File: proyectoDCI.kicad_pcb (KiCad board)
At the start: 2 copper layers, 27 parts, among them IC1 AG849, IC2 AD5933, IC3 ASFLMB-16.000MHZ-LY-T, IC4 ADP150, P1 GSG-RF-CONN, P2 GSG-RF-CONN, P3 CONN_02X04, P4 CONN_01X01, U1 AD8606

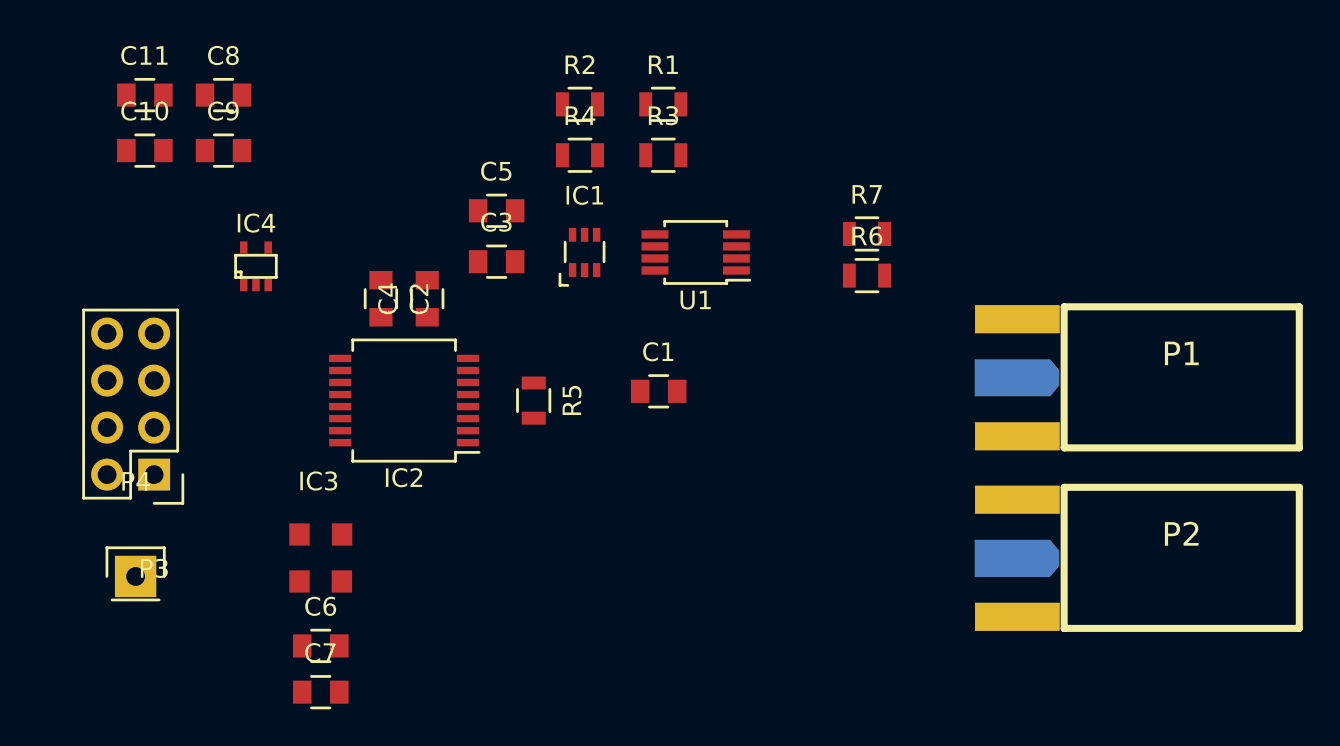
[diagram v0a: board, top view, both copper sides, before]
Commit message: Reformulado el esquematico para contener el diseño en dos hojas
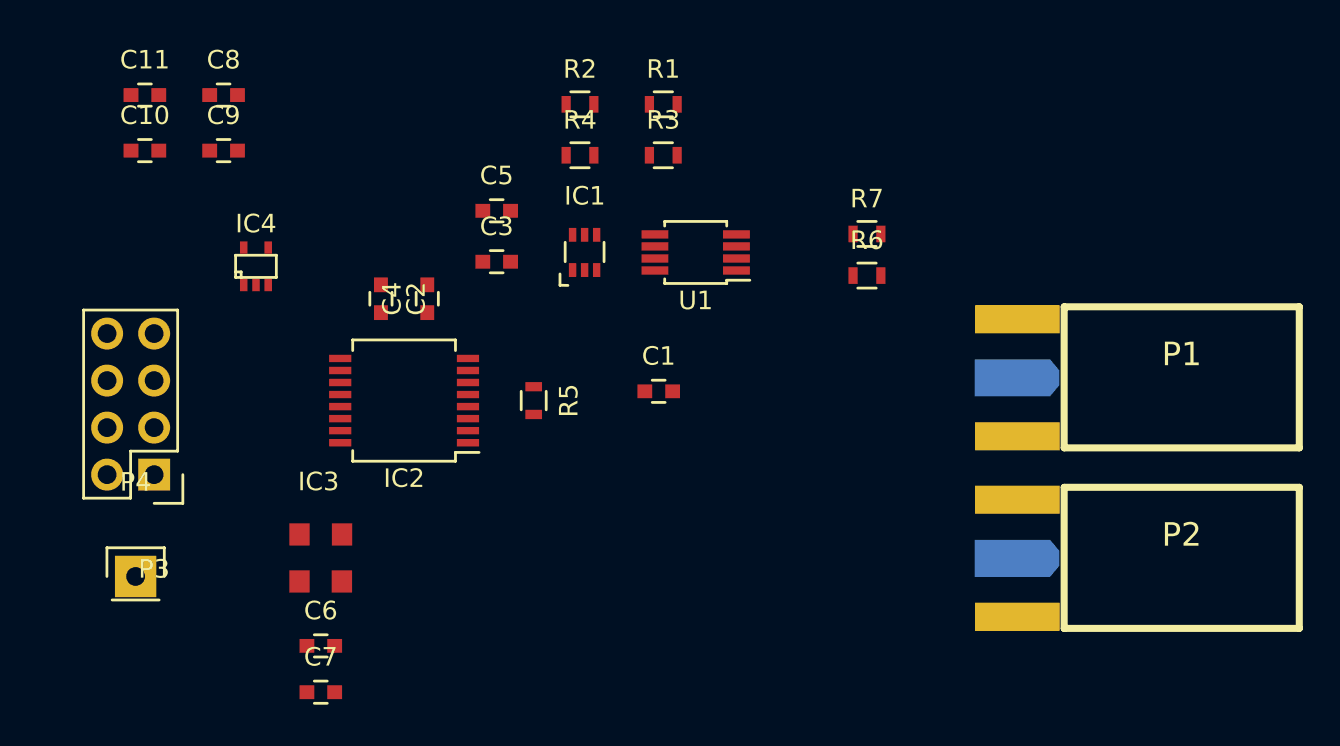
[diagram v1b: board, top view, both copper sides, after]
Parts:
- C1, C10, C11, C2, C3, C4, C5, C6, C7, C8, C9: footprint Capacitors_SMD:C_0805 -> Capacitors_SMD:C_0603
- R1, R2, R3, R4, R5, R6, R7: footprint Resistors_SMD:R_0805 -> Resistors_SMD:R_0603

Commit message: Problema de footprints solucionado
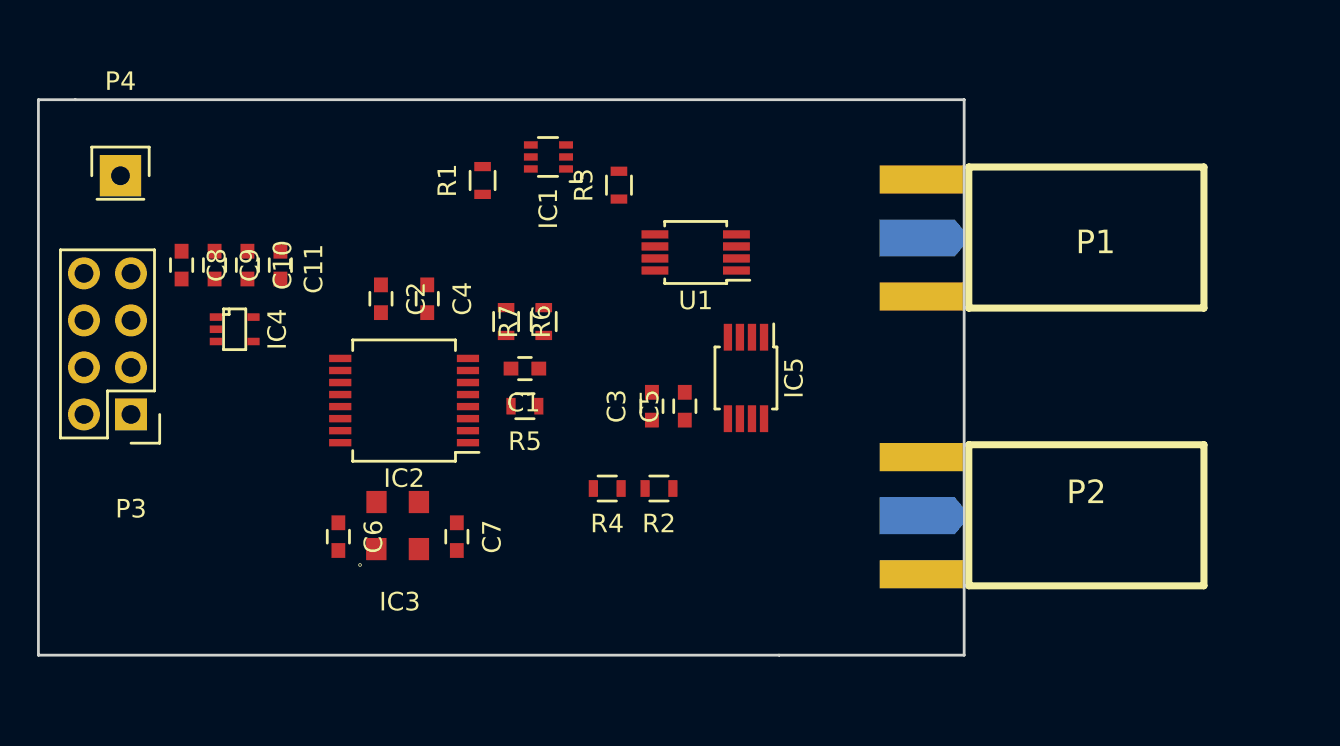
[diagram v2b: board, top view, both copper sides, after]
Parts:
- added IC5: AD8606, Housings_SSOP:MSOP-8_3x3mm_Pitch0.65mm, F.Cu at (188.2, 113.0)
- IC1: value AG849 -> ADG849
- IC3: footprint propios:TCXO -> TCXO
- moved P4 21.7 mm to (154.4, 102.1)
- moved R2 21.2 mm to (183.5, 119.0), turned to 180 degrees
- moved R6 19.6 mm to (175.3, 110.0), turned to 270 degrees
- moved R7 18.1 mm to (177.3, 110.0), turned to 90 degrees
- moved R4 18.1 mm to (180.7, 119.0), turned to 180 degrees
- moved C5 14.7 mm to (184.9, 114.6), turned to 90 degrees
- moved C11 11.7 mm to (163.1, 106.9), turned to 270 degrees
- moved C3 11.5 mm to (183.1, 114.6), turned to 90 degrees
- moved C7 11.2 mm to (172.6, 121.6), turned to 270 degrees
- moved R1 10.6 mm to (174.0, 102.4), turned to 90 degrees
- moved C8 9.46 mm to (157.7, 106.9), turned to 270 degrees
- moved P1 9.14 mm to (206.6, 104.2)
- moved C10 8.30 mm to (161.3, 106.9), turned to 270 degrees
- moved C1 7.33 mm to (176.3, 112.5), turned to 180 degrees
- moved C9 6.20 mm to (159.5, 106.9), turned to 270 degrees
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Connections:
- net Net-(C1-Pad2) renamed /Senal/VOUT
- net Net-(IC1-Pad4) renamed /Senal/S1
- net Net-(IC1-Pad6) renamed /Senal/S2
- net Net-(IC2-Pad4) renamed /Senal/RFB
- C1 pad 1: Net-(C1-Pad1) -> /Senal/VOUT_D
- IC1 pad 5: Net-(IC1-Pad5) -> /Senal/VIN
- IC2 pad 5: Net-(IC1-Pad5) -> /Senal/VIN
- IC2 pad 8: /Reloj/MCLK -> /Otros/MCLK
- P1 pad 1: Net-(P1-Pad1) -> /Senal/CIN
- P2 pad 1: Net-(P2-Pad1) -> /Senal/COUT
- P3 pad 7: VDD -> /Senal/VCC
- P3 pad 8: VDD -> /Senal/VCC
- R1 pad 2: Net-(P1-Pad1) -> /Senal/CIN
- R2 pad 2: Net-(R2-Pad2) -> /Senal/VREF
- R3 pad 2: Net-(P1-Pad1) -> /Senal/CIN
- R4 pad 1: Net-(R2-Pad2) -> /Senal/VREF
- R5 pad 1: Net-(IC1-Pad5) -> /Senal/VIN
- R6 pad 2: Net-(C1-Pad1) -> /Senal/VOUT_D
- R7 pad 1: Net-(C1-Pad1) -> /Senal/VOUT_D
- U1 pad 1: Net-(P2-Pad1) -> (no net)
- U1 pad 2: Net-(P2-Pad1) -> (no net)
- U1 pad 3: Net-(C1-Pad1) -> (no net)
- U1 pad 5: Net-(P1-Pad1) -> (no net)
- U1 pad 6: Net-(R2-Pad2) -> (no net)
- U1 pad 7: Net-(IC1-Pad5) -> (no net)
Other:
- board outline added: 50 x 30 mm
- board text added: "Fuente"
- board text added: "Reloj"

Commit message: Sectorizacion terminada
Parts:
- removed IC1: ADG849, TO_SOT_Packages_SMD:SC-70-6
- removed IC2: AD5933, Housings_SSOP:SSOP-16_5.3x6.2mm_Pitch0.65mm
- removed IC3: ASFLMB-16.000MHZ-LY-T, TCXO
- removed IC4: ADP150, TO_SOT_Packages_SMD:SC-70-5
- removed IC5: AD8606, Housings_SSOP:MSOP-8_3x3mm_Pitch0.65mm
- added U2: ADG849, TO_SOT_Packages_SMD:SC-70-6, F.Cu at (177.3, 102.6)
- added U3: AD8606, Housings_SSOP:MSOP-8_3x3mm_Pitch0.65mm, F.Cu at (184.7, 107.2)
- added U4: ASFLMB-16.000MHZ-LY-T, propios:TCXO, F.Cu at (169.4, 121.4)
- added U5: ADP150, TO_SOT_Packages_SMD:SC-70-5, F.Cu at (160.5, 110.5)
- C10, C8: value 10uF -> 0,1uF
- C6, C9: value 0,1uF -> 10uF
- P1: value GSG-RF-CONN -> CONN_02X04; footprint SMA_EDGE:SMA_EDGE -> Pin_Headers:Pin_Header_Straight_2x04
- P2: value GSG-RF-CONN -> CONN_01X01; footprint SMA_EDGE:SMA_EDGE -> Pin_Headers:Pin_Header_Straight_1x01
- P3: value CONN_02X04 -> GSG-RF-CONN; footprint Pin_Headers:Pin_Header_Straight_2x04 -> SMA_EDGE:SMA_EDGE
- P4: value CONN_01X01 -> GSG-RF-CONN; footprint Pin_Headers:Pin_Header_Straight_1x01 -> SMA_EDGE:SMA_EDGE
- U1: value AD8606 -> AD5933; footprint Housings_SSOP:MSOP-8_3x3mm_Pitch0.65mm -> Housings_SSOP:SSOP-16_5.3x6.2mm_Pitch0.65mm
- moved P2 56.4 mm to (152.9, 101.9)
- moved P4 54.8 mm to (206.5, 119.1)
- moved P1 54.6 mm to (152.1, 108.2)
- moved P3 52.4 mm to (206.2, 104.1), turned to 0 degrees
- moved U1 17.4 mm to (169.9, 114.0)
- moved R4 17.0 mm to (186.2, 102.9), turned to 0 degrees
- moved C5 16.9 mm to (173.0, 102.6), turned to 270 degrees
- moved R2 16.1 mm to (183.4, 102.9), turned to 0 degrees
- moved C3 14.6 mm to (174.8, 102.6), turned to 270 degrees
- moved R7 9.37 mm to (186.4, 112.0), turned to 0 degrees
- moved R6 8.62 mm to (183.6, 112.0), turned to 0 degrees
- moved R3 6.06 mm to (176.3, 105.9), turned to 270 degrees
- moved R1 5.59 mm to (178.3, 105.9), turned to 270 degrees
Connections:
- C10 pad 1: VAA -> /Otros/MCLK
- C7 pad 1: /Reloj/MCLK -> VDD
- C9 pad 1: VDD -> VAA
- P1 pad 1: /Senal/CIN -> /Senal/SCL
- P1 pad 2: GND -> /Senal/SCL
- P2 pad 1: /Senal/COUT -> /Senal/SEL
- P3 pad 1: /Senal/SCL -> /Senal/CIN
- P3 pad 2: /Senal/SCL -> GND
- P4 pad 1: /Senal/SEL -> /Senal/COUT
- U1 pad 4: GND -> /Senal/RFB
- U1 pad 5: (no net) -> /Senal/VIN
- U1 pad 6: (no net) -> /Senal/VOUT
- U1 pad 8: VAA -> /Otros/MCLK
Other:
- board text added: "OPAMP"
- board text added: "SPDT"
